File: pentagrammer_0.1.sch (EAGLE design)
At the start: 20 parts, among them CON1 AVR-ISP-6, IC1 AT90S2313P

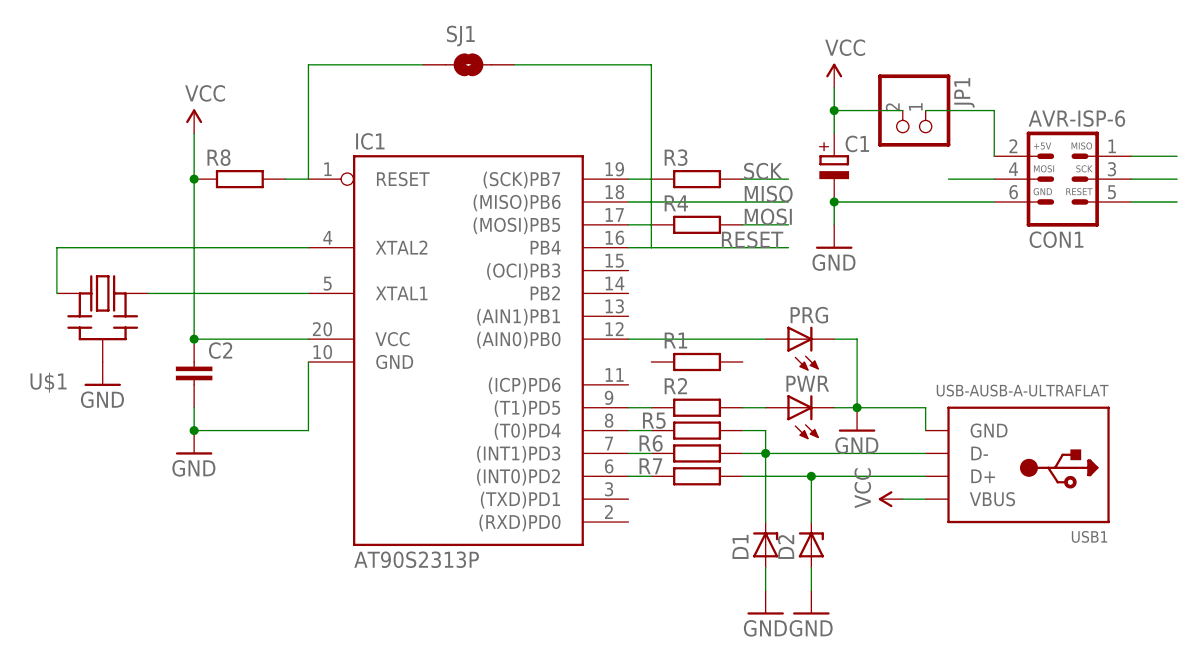
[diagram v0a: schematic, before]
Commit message: added values for resistors
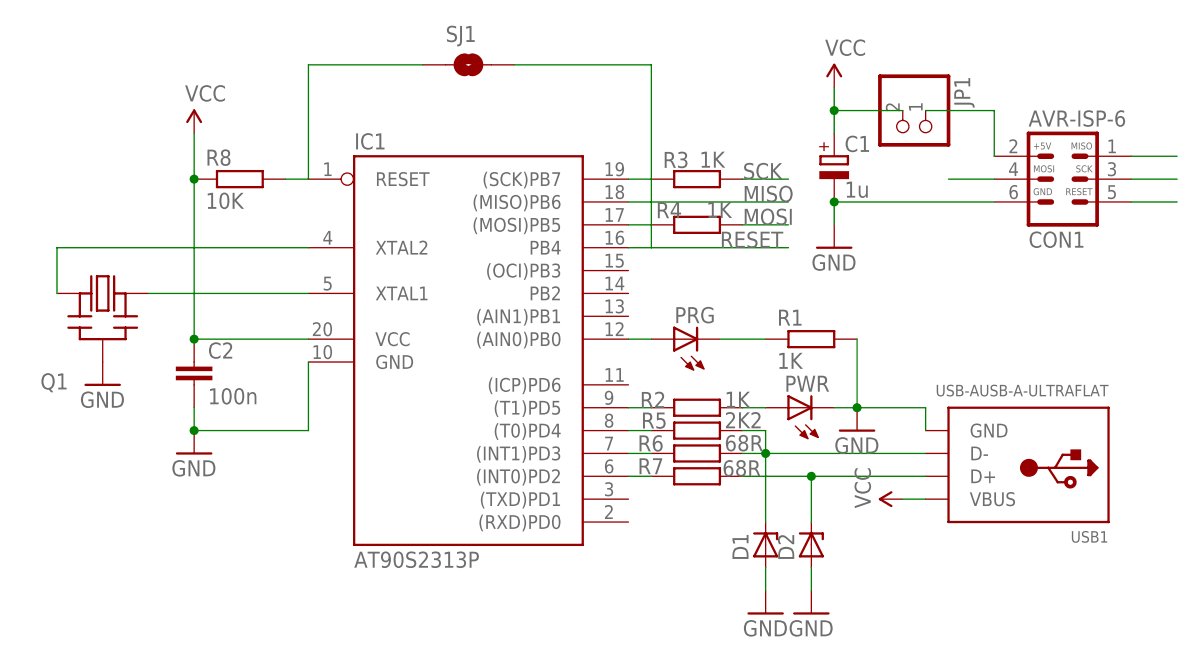
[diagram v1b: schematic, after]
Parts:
- C1: value (none) -> 1u
- C2: value (none) -> 100n
- R1, R2, R3, R4: value (none) -> 1K
- R5: value (none) -> 2K2
- R6, R7: value (none) -> 68R
- R8: value (none) -> 10K
- renumbered U$1 to Q1
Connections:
- new net N$15: PRG.C, R1.1
- net GND: now also R1.2; no longer PRG.C
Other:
- moved on the sheet: PRG, R1
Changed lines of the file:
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@@
 <?xml version="1.0" encoding="utf-8"?>
 <!DOCTYPE eagle SYSTEM "eagle.dtd">
-<eagle version="6.5.0">
+<eagle version="6.6.0">
 <drawing>
 <settings>
@@
 <parts>
 <part name="IC1" library="atmel" deviceset="AT90S2313" device="P"/>
-<part name="C1" library="rcl" deviceset="CPOL-EU" device="E1.8-4"/>
+<part name="C1" library="rcl" deviceset="CPOL-EU" device="E1.8-4" value="1u"/>
 <part name="USB1" library="bigalexeasysolder" deviceset="USB-A" device="USB-A-ULTRAFLAT"/>
 <part name="PWR" library="adafruit" deviceset="LED" device="3MM"/>
 <part name="PRG" library="adafruit" deviceset="LED" device="3MM"/>
-<part name="R1" library="rcl" deviceset="R-EU_" device="0204/7"/>
+<part name="R1" library="rcl" deviceset="R-EU_" device="0204/7" value="1K"/>
 <part name="CON1" library="bigalexeasysolder" deviceset="AVR-ISP-6" device=""/>
-<part name="U$1" library="adafruit" deviceset="CERMOSCILL" device="-THM"/>
+<part name="Q1" library="adafruit" deviceset="CERMOSCILL" device="-THM"/>
 <part name="GND1" library="SparkFun" deviceset="GND" device=""/>
 <part name="GND2" library="SparkFun" deviceset="GND" device=""/>
@@
 <part name="D1" library="diode" deviceset="ZENER-DIODE" device="ZD-5"/>
 <part name="D2" library="diode" deviceset="ZENER-DIODE" device="ZD-5"/>
-<part name="R2" library="rcl" deviceset="R-EU_" device="0204/7"/>
-<part name="R3" library="rcl" deviceset="R-EU_" device="0204/7"/>
-<part name="R4" library="rcl" deviceset="R-EU_" device="0204/7"/>
-<part name="R5" library="rcl" deviceset="R-EU_" device="0204/7"/>
-<part name="R6" library="rcl" deviceset="R-EU_" device="0204/7"/>
-<part name="R7" library="rcl" deviceset="R-EU_" device="0204/7"/>
-<part name="R8" library="rcl" deviceset="R-EU_" device="0204/7"/>
+<part name="R2" library="rcl" deviceset="R-EU_" device="0204/7" value="1K"/>
+<part name="R3" library="rcl" deviceset="R-EU_" device="0204/7" value="1K"/>
+<part name="R4" library="rcl" deviceset="R-EU_" device="0204/7" value="1K"/>
+<part name="R5" library="rcl" deviceset="R-EU_" device="0204/7" value="2K2"/>
+<part name="R6" library="rcl" deviceset="R-EU_" device="0204/7" value="68R"/>
+<part name="R7" library="rcl" deviceset="R-EU_" device="0204/7" value="68R"/>
+<part name="R8" library="rcl" deviceset="R-EU_" device="0204/7" value="10K"/>
 <part name="GND4" library="SparkFun" deviceset="GND" device=""/>
 <part name="GND5" library="SparkFun" deviceset="GND" device=""/>
 <part name="P+2" library="SparkFun" deviceset="VCC" device=""/>
 <part name="P+3" library="SparkFun" deviceset="VCC" device=""/>
-<part name="C2" library="rcl" deviceset="C-EU" device="025-024X044"/>
+<part name="C2" library="rcl" deviceset="C-EU" device="025-024X044" value="100n"/>
 <part name="GND7" library="SparkFun" deviceset="GND" device=""/>
 <part name="SJ1" library="SparkFun" deviceset="SOLDERJUMPER" device="NO"/>
@@
 <instance part="USB1" gate="G$1" x="124.46" y="38.1" rot="R180"/>
 <instance part="PWR" gate="G$1" x="99.06" y="43.18" rot="R90"/>
-<instance part="PRG" gate="G$1" x="99.06" y="50.8" rot="R90"/>
-<instance part="R1" gate="G$1" x="88.9" y="48.26"/>
+<instance part="PRG" gate="G$1" x="86.36" y="50.8" rot="R90"/>
+<instance part="R1" gate="G$1" x="101.6" y="50.8"/>
 <instance part="CON1" gate="1" x="129.54" y="68.58"/>
-<instance part="U$1" gate="G$1" x="22.86" y="50.8"/>
+<instance part="Q1" gate="G$1" x="22.86" y="50.8"/>
 <instance part="GND1" gate="1" x="106.68" y="40.64"/>
 <instance part="GND2" gate="1" x="22.86" y="45.72"/>
@@
 <instance part="D1" gate="G$1" x="96.52" y="27.94" rot="R90"/>
 <instance part="D2" gate="G$1" x="101.6" y="27.94" rot="R90"/>
-<instance part="R2" gate="G$1" x="88.9" y="43.18"/>
-<instance part="R3" gate="G$1" x="88.9" y="68.58"/>
-<instance part="R4" gate="G$1" x="88.9" y="63.5"/>
+<instance part="R2" gate="G$1" x="88.9" y="43.18" smashed="yes">
+<attribute name="NAME" x="82.55" y="43.1546" size="1.778" layer="95"/>
+<attribute name="VALUE" x="91.948" y="43.18" size="1.778" layer="96"/>
+</instance>
+<instance part="R3" gate="G$1" x="88.9" y="68.58" smashed="yes">
+<attribute name="NAME" x="85.09" y="69.8246" size="1.778" layer="95"/>
+<attribute name="VALUE" x="89.154" y="69.85" size="1.778" layer="96"/>
+</instance>
+<instance part="R4" gate="G$1" x="88.9" y="63.5" smashed="yes">
+<attribute name="NAME" x="84.328" y="64.2366" size="1.778" layer="95"/>
+<attribute name="VALUE" x="89.916" y="64.262" size="1.778" layer="96"/>
+</instance>
 <instance part="R5" gate="G$1" x="88.9" y="40.64" smashed="yes">
 <attribute name="NAME" x="85.598" y="40.8686" size="1.778" layer="95" rot="MR0"/>
-<attribute name="VALUE" x="85.09" y="37.338" size="1.778" layer="96"/>
+<attribute name="VALUE" x="91.948" y="40.894" size="1.778" layer="96"/>
 </instance>
 <instance part="R6" gate="G$1" x="88.9" y="38.1" smashed="yes">
 <attribute name="NAME" x="82.296" y="38.3286" size="1.778" layer="95"/>
-<attribute name="VALUE" x="85.09" y="34.798" size="1.778" layer="96"/>
+<attribute name="VALUE" x="91.948" y="38.354" size="1.778" layer="96"/>
 </instance>
 <instance part="R7" gate="G$1" x="88.9" y="35.56" smashed="yes">
 <attribute name="NAME" x="82.296" y="35.7886" size="1.778" layer="95"/>
-<attribute name="VALUE" x="85.09" y="32.258" size="1.778" layer="96"/>
+<attribute name="VALUE" x="91.694" y="35.56" size="1.778" layer="96"/>
 </instance>
 <instance part="R8" gate="G$1" x="38.1" y="68.58"/>
@@
 <net name="N$3" class="0">
 <segment>
-<pinref part="U$1" gate="G$1" pin="IN"/>
+<pinref part="Q1" gate="G$1" pin="IN"/>
 <pinref part="IC1" gate="G$1" pin="XTAL2"/>
 <wire x1="17.78" y1="55.88" x2="17.78" y2="60.96" width="0.1524" layer="91"/>
@@
 <segment>
 <pinref part="IC1" gate="G$1" pin="XTAL1"/>
-<pinref part="U$1" gate="G$1" pin="OUT"/>
+<pinref part="Q1" gate="G$1" pin="OUT"/>
 <wire x1="45.72" y1="55.88" x2="27.94" y2="55.88" width="0.1524" layer="91"/>
 </segment>
@@
 <pinref part="IC1" gate="G$1" pin="(AIN0)PB0"/>
 <pinref part="PRG" gate="G$1" pin="A"/>
-<wire x1="81.28" y1="50.8" x2="96.52" y2="50.8" width="0.1524" layer="91"/>
+<wire x1="81.28" y1="50.8" x2="83.82" y2="50.8" width="0.1524" layer="91"/>
 </segment>
 </net>
 <net name="GND" class="0">
 <segment>
-<pinref part="U$1" gate="G$1" pin="GND"/>
+<pinref part="Q1" gate="G$1" pin="GND"/>
 <pinref part="GND2" gate="1" pin="GND"/>
 </segment>
@@
 <pinref part="GND1" gate="1" pin="GND"/>
 <wire x1="104.14" y1="43.18" x2="106.68" y2="43.18" width="0.1524" layer="91"/>
-<pinref part="PRG" gate="G$1" pin="C"/>
-<wire x1="104.14" y1="50.8" x2="106.68" y2="50.8" width="0.1524" layer="91"/>
 <wire x1="106.68" y1="50.8" x2="106.68" y2="43.18" width="0.1524" layer="91"/>
 <junction x="106.68" y="43.18"/>
@@
 <wire x1="114.3" y1="40.64" x2="114.3" y2="43.18" width="0.1524" layer="91"/>
 <wire x1="114.3" y1="43.18" x2="106.68" y2="43.18" width="0.1524" layer="91"/>
+<pinref part="R1" gate="G$1" pin="2"/>
 </segment>
 <segment>
@@
 </segment>
 </net>
+<net name="N$15" class="0">
+<segment>
+<pinref part="PRG" gate="G$1" pin="C"/>
+<pinref part="R1" gate="G$1" pin="1"/>
+<wire x1="96.52" y1="50.8" x2="91.44" y2="50.8" width="0.1524" layer="91"/>
+</segment>
+</net>
